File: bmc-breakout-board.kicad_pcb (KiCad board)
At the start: 4 copper layers, 90 x 60 mm, 23 parts, among them J1 PinHeader_2x4, J10 PinHeader_2x4, J11 PinHeader_2x05, J12 61300411121, J13 0473460001, J14 PCIE_BUS_x1, J15 0473460001, J16 PinHeader_1x07, J2 PinHeader_2x13, J3 PinHeader_2x08, J4 61300411121, J5 ME1016813401101, J6 61300411121, J7 DC_SOCKET, J8 PinHeader_2x05, J9 PinHeader_1x07, Q1 BSS138AKA

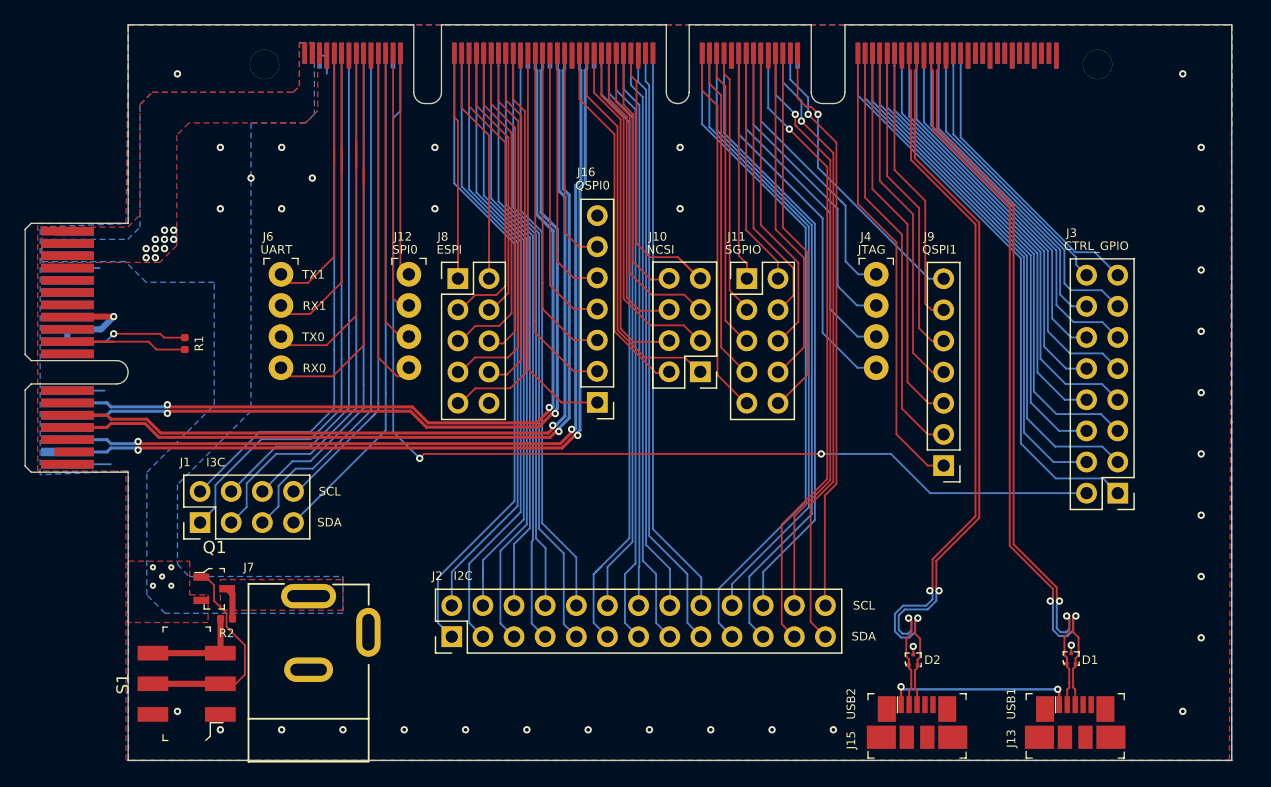
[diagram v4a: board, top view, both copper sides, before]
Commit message: Add mounting holes
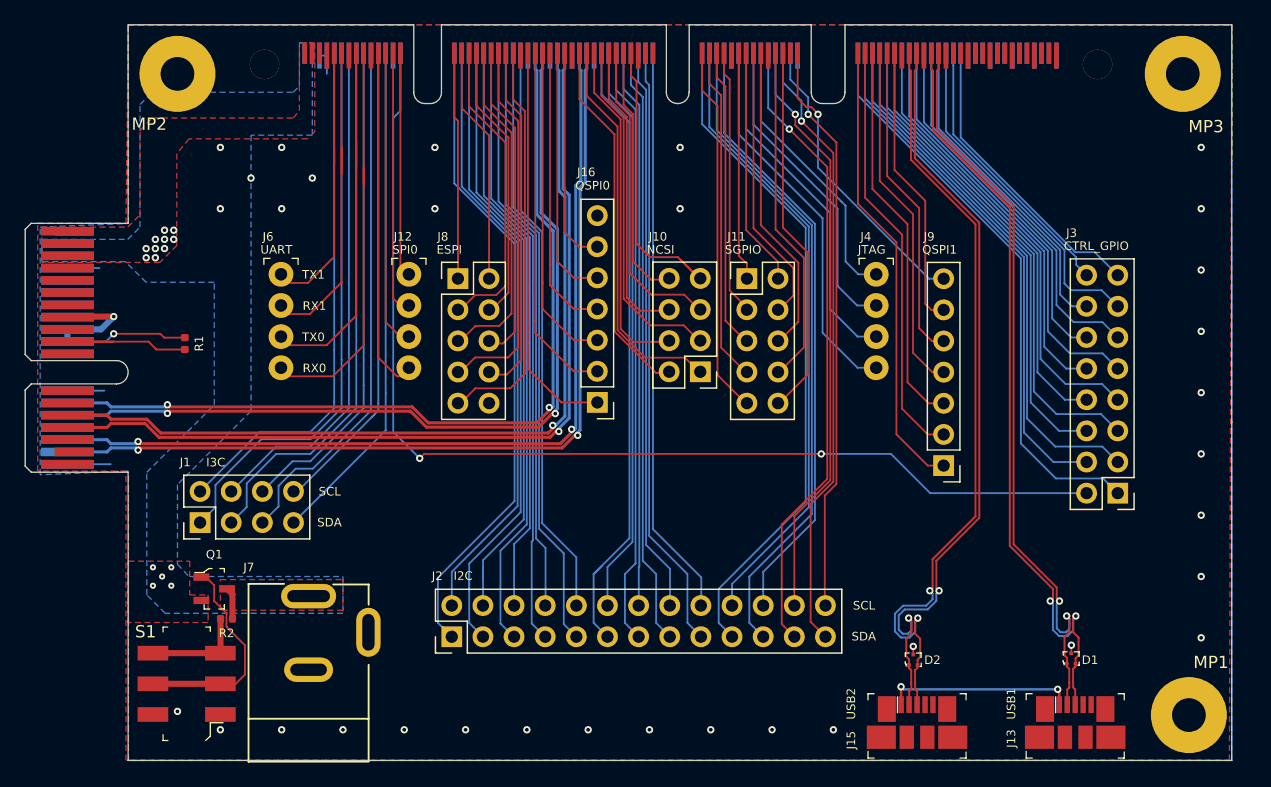
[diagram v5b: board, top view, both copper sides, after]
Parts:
- added MP1: PCB_Mount_Hole_2.5_6.2, bmc-breakout-board-footprints:Mount-hole-M2.5, F.Cu at (146.6, 119.0)
- added MP2: PCB_Mount_Hole_2.5_6.2, bmc-breakout-board-footprints:Mount-hole-M2.5, F.Cu at (64.1, 66.7)
- added MP3: PCB_Mount_Hole_2.5_6.2, bmc-breakout-board-footprints:Mount-hole-M2.5, F.Cu at (146.1, 66.7)
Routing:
- net GND: vias 36 -> 30
- net (no net): vias 0 -> 3
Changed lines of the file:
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@@
     (thickness 1.55)
     (drawings 121)
-    (tracks 905)
+    (tracks 902)
     (zones 0)
-    (modules 23)
+    (modules 26)
     (nets 159)
   )
@@
     (add_net USB2_D_P)
   )
+  (module bmc-breakout-board-footprints:Mount-hole-M2.5 (layer F.Cu)
+    (at 146.1 66.665)
+    (fp_text reference MP3 (at 1.9 4.3) (layer F.SilkS)
+      (effects (font (size 1 1) (thickness 0.15)))
+    )
+    (fp_text value PCB_Mount_Hole_2.5_6.2 (at 0 -0.5) (layer F.Fab)
+      (effects (font (size 1 1) (thickness 0.15)))
+    )
+    (pad 1 thru_hole circle (at 0 0) (size 6.2 6.2) (drill 2.75) (layers *.Cu *.Mask))
+  )
+  (module bmc-breakout-board-footprints:Mount-hole-M2.5 (layer F.Cu)
+    (at 64.1 66.665)
+    (fp_text reference MP2 (at -2.3 4.1) (layer F.SilkS)
+      (effects (font (size 1 1) (thickness 0.15)))
+    )
+    (fp_text value PCB_Mount_Hole_2.5_6.2 (at 0 -0.5) (layer F.Fab)
+      (effects (font (size 1 1) (thickness 0.15)))
+    )
+    (pad 1 thru_hole circle (at 0 0) (size 6.2 6.2) (drill 2.75) (layers *.Cu *.Mask))
+  )
+  (module bmc-breakout-board-footprints:Mount-hole-M2.5 (layer F.Cu)
+    (at 146.6 118.965)
+    (fp_text reference MP1 (at 1.8 -4.3) (layer F.SilkS)
+      (effects (font (size 1 1) (thickness 0.15)))
+    )
+    (fp_text value PCB_Mount_Hole_2.5_6.2 (at 0 -0.5) (layer F.Fab)
+      (effects (font (size 1 1) (thickness 0.15)))
+    )
+    (pad 1 thru_hole circle (at 0 0) (size 6.2 6.2) (drill 2.75) (layers *.Cu *.Mask))
+  )
   (module bmc-breakout-board-footprints:Switch_Slide_JS202011SCQN (layer F.Cu)
     (at 64.85 116.415 90)
     (attr smd)
-    (fp_text reference S1 (at 0 -5.2 90) (layer F.SilkS)
+    (fp_text reference S1 (at 4.25 -3.35 180) (layer F.SilkS)
       (effects (font (size 1 1) (thickness 0.15)))
     )
@@
     (at 67.1 108.665)
     (attr smd)
-    (fp_text reference Q1 (at 0.025 -3.375) (layer F.SilkS)
-      (effects (font (size 1 1) (thickness 0.15)))
+    (fp_text reference Q1 (at 0 -2.8) (layer F.SilkS)
+      (effects (font (size 0.7 0.7) (thickness 0.15)))
     )
     (fp_text value BSS138AKA (at 0.025 3.25) (layer F.Fab)
@@
   (gr_line (start 83.375 62.665) (end 60.075 62.665) (layer Edge.Cuts) (width 0.05))
   (gr_line (start 109.939 122.517) (end 118.929 122.517) (layer B.SilkS) (width 0.12))
-  (via (at 146.1 66.665) (size 0.6) (drill 0.3) (layers F.Cu B.Cu) (net 1))
-  (via (at 146.1 118.665) (size 0.6) (drill 0.3) (layers F.Cu B.Cu) (net 1))
   (via (at 64.1 118.665) (size 0.6) (drill 0.3) (layers F.Cu B.Cu) (net 1))
-  (via (at 64.1 66.665) (size 0.6) (drill 0.3) (layers F.Cu B.Cu) (net 1))
   (via (at 147.6 77.665) (size 0.6) (drill 0.3) (layers F.Cu B.Cu) (net 1))
   (via (at 147.6 82.665) (size 0.6) (drill 0.3) (layers F.Cu B.Cu) (net 1))
@@
   (via (at 67.6 120.165) (size 0.6) (drill 0.3) (layers F.Cu B.Cu) (net 1))
   (via (at 72.6 120.165) (size 0.6) (drill 0.3) (layers F.Cu B.Cu) (net 1))
-  (via (at 67.6 72.665) (size 0.6) (drill 0.3) (layers F.Cu B.Cu) (net 1))
+  (via (at 67.6 72.665) (size 0.6) (drill 0.3) (layers F.Cu B.Cu) (net 0))
   (via (at 72.6 72.665) (size 0.6) (drill 0.3) (layers F.Cu B.Cu) (net 1))
-  (via (at 70.1 75.165) (size 0.6) (drill 0.3) (layers F.Cu B.Cu) (net 1))
+  (via (at 70.1 75.165) (size 0.6) (drill 0.3) (layers F.Cu B.Cu) (net 0))
   (via (at 75.1 75.165) (size 0.6) (drill 0.3) (layers F.Cu B.Cu) (net 1))
-  (via (at 67.6 77.665) (size 0.6) (drill 0.3) (layers F.Cu B.Cu) (net 1))
+  (via (at 67.6 77.665) (size 0.6) (drill 0.3) (layers F.Cu B.Cu) (net 0))
   (via (at 72.6 77.665) (size 0.6) (drill 0.3) (layers F.Cu B.Cu) (net 1))
   (via (at 105.1 77.665) (size 0.6) (drill 0.3) (layers F.Cu B.Cu) (net 1))
@@
     (polygon
       (pts
-        (xy 75.27 69.948648) (xy 74.545 70.665) (xy 70.1 70.665) (xy 70.1 94.165) (xy 64.1 100.165)
-        (xy 64.1 106.665) (xy 65.045 107.665) (xy 77.6 107.665) (xy 77.6 110.665) (xy 63.1 110.665)
-        (xy 61.6 109.165) (xy 61.6 99.165) (xy 67.1 93.665) (xy 67.1 83.665) (xy 61.545 83.665)
-        (xy 59.85 81.975) (xy 53.045 81.975) (xy 53.045 80.165) (xy 60.045 80.165) (xy 61.045 79.165)
-        (xy 61.045 69.165) (xy 62.045 68.165) (xy 73.545 68.165) (xy 74.045 67.665) (xy 74.05 64.115)
-        (xy 75.27 64.115)
+        (xy 75.1 71.665) (xy 70.1 71.665) (xy 70.1 94.165) (xy 64.1 100.165) (xy 64.1 106.665)
+        (xy 65.045 107.665) (xy 77.6 107.665) (xy 77.6 110.665) (xy 63.1 110.665) (xy 61.6 109.165)
+        (xy 61.6 99.165) (xy 67.1 93.665) (xy 67.1 83.665) (xy 61.545 83.665) (xy 59.85 81.975)
+        (xy 53.045 81.975) (xy 53.045 80.165) (xy 60.045 80.165) (xy 61.045 79.165) (xy 61.045 69.165)
+        (xy 62.045 68.165) (xy 73.545 68.165) (xy 74.045 67.665) (xy 74.05 64.115) (xy 75.1 64.115)
       )
     )
@@
     (polygon
       (pts
-        (xy 75.545 69.665) (xy 74.545 70.665) (xy 65.045 70.665) (xy 64.045 71.665) (xy 64.045 80.665)
+        (xy 75.3 71.365) (xy 74.7 71.965) (xy 65.045 71.965) (xy 64.045 73.165) (xy 64.045 80.665)
         (xy 62.66 82.045) (xy 53.045 82.045) (xy 53.045 79.165) (xy 60.045 79.165) (xy 61.045 78.165)
-        (xy 61.045 69.165) (xy 62.045 68.165) (xy 73.545 68.165) (xy 74.045 67.665) (xy 74.045 64.165)
-        (xy 75.545 64.165)
+        (xy 61.045 71.265) (xy 62.045 70.265) (xy 73.545 70.265) (xy 74.045 69.665) (xy 74.045 64.165)
+        (xy 75.3 64.165)
       )
     )

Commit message: Add descriptions on the silkscreen layer
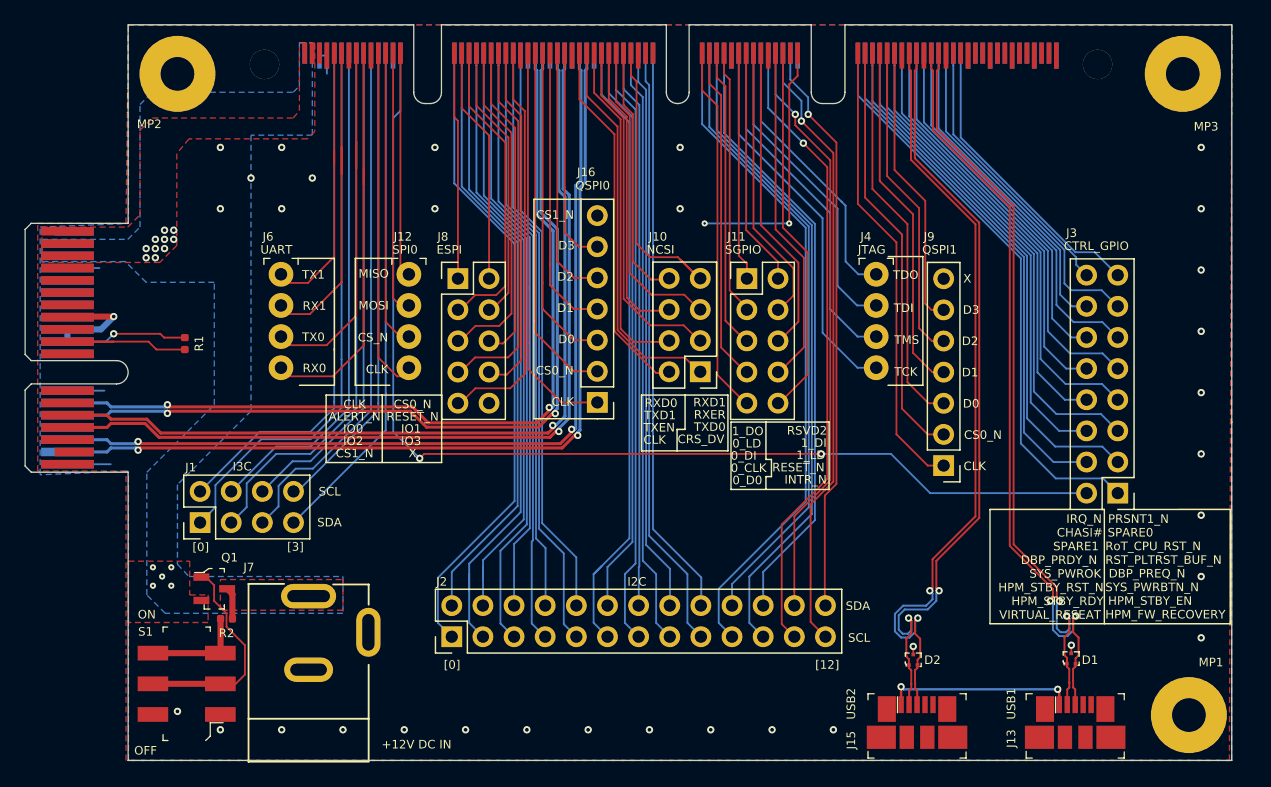
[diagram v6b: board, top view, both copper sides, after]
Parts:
- MP1, MP2, MP3: footprint bmc-breakout-board-footprints:Mount-hole-M2.5 -> antmicro-footprints:Mount-hole-M2.5
- Q1: footprint bmc-breakout-board-footprints:SOT-23-3 -> antmicro-footprints:SOT-23-3
- R2: footprint bmc-breakout-board-footprints:0402-res -> antmicro-footprints:0402-res
- S1: footprint bmc-breakout-board-footprints:Switch_Slide_JS202011SCQN -> antmicro-footprints:Switch_Slide_JS202011SCQN
- moved N1 1.88 mm to (94.5, 102.5)
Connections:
- J16 pad 7: Net-(J16-Pad7) -> QSPI0_CS1_N
- J9 pad 7: QSPI0_CS1_N -> Net-(J9-Pad7)
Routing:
- net QSPI0_CS1_N: track 24.3 -> 30.1 mm, vias 1 -> 2
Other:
- board text added: "+12V DC IN"
- board text added: "0_CLK"
- board text added: "0_D0"
- board text added: "0_DI"
- board text added: "0_LD"
- board text added: "1_DI"
- board text added: "1_DO"
- board text added: "1_LD"
- board text added: "ALERT_N"
- board text added: "CHASI#"
- board text added: "CLK"
- board text added: "CRS_DV"
- board text added: "CS0_N"
- board text added: "CS1_N"
- board text added: "CS_N"
- board text added: "D0"
- board text added: "D1"
- board text added: "D2"
- board text added: "D3"
- board text added: "DBP_PRDY_N"
- board text added: "DBP_PREQ_N"
- board text added: "HPM_FW_RECOVERY"
- board text added: "HPM_STBY_EN"
- board text added: "HPM_STBY_RDY"
- board text added: "HPM_STBY_RST_N"
- board text added: "INTR_N"
- board text added: "IO0"
- board text added: "IO1"
- board text added: "IO2"
- board text added: "IO3"
- board text added: "IRQ_N"
- board text added: "MISO"
- board text added: "MOSI"
- board text added: "OFF"
- board text added: "ON"
- board text added: "PRSNT1_N"
- board text added: "RESET_N"
- board text added: "RST_PLTRST_BUF_N"
- board text added: "RSVD2"
- board text added: "RXD0"
- board text added: "RXD1"
- board text added: "RXER"
- board text added: "RoT_CPU_RST_N"
- board text added: "SPARE0"
- board text added: "SPARE1"
- board text added: "SYS_PWRBTN_N"
- board text added: "SYS_PWROK"
- board text added: "TCK"
- board text added: "TDI"
- board text added: "TDO"
- board text added: "TMS"
- board text added: "TXD0"
- board text added: "TXD1"
- board text added: "TXEN"
- board text added: "VIRTUAL_RESEAT"
- board text added: "X"
- board text added: "[0]"
- board text added: "[12]"
- board text added: "[3]"

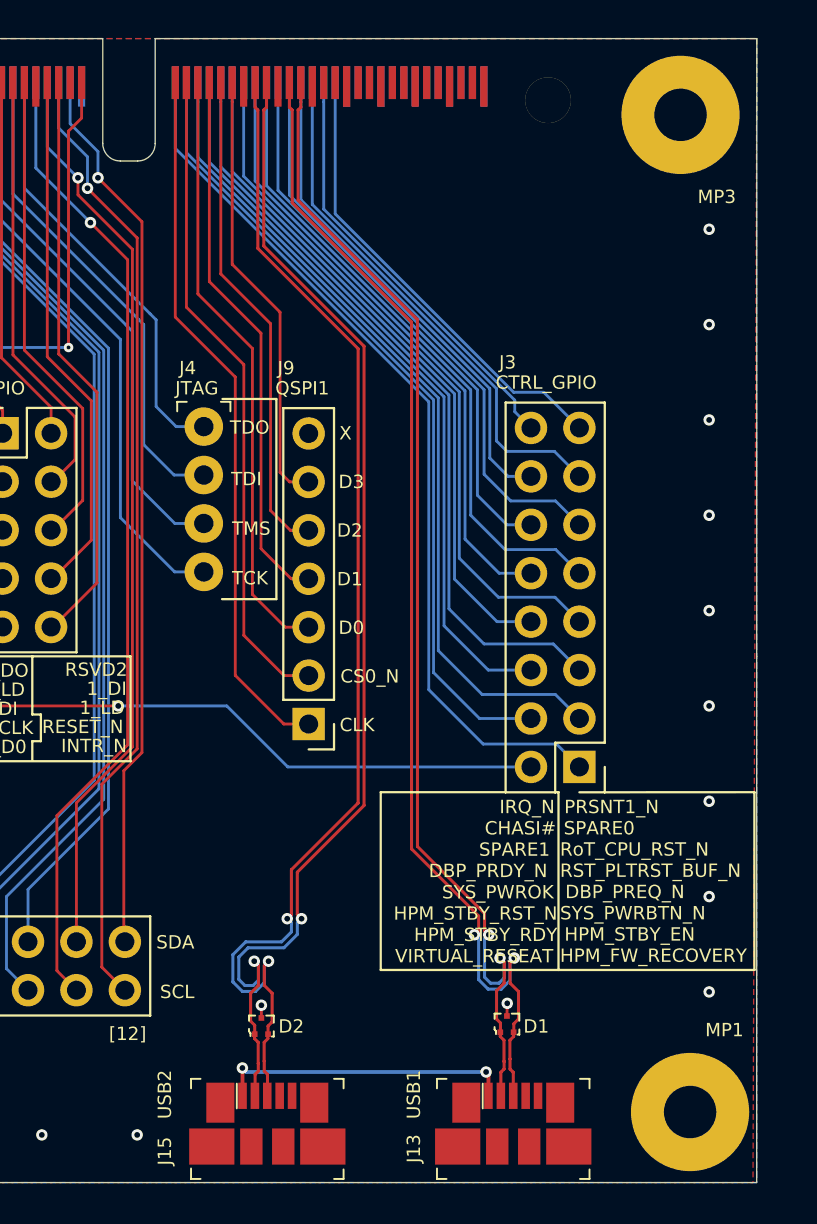
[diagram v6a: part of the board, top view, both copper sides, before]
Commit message: Replace host USB with USB A
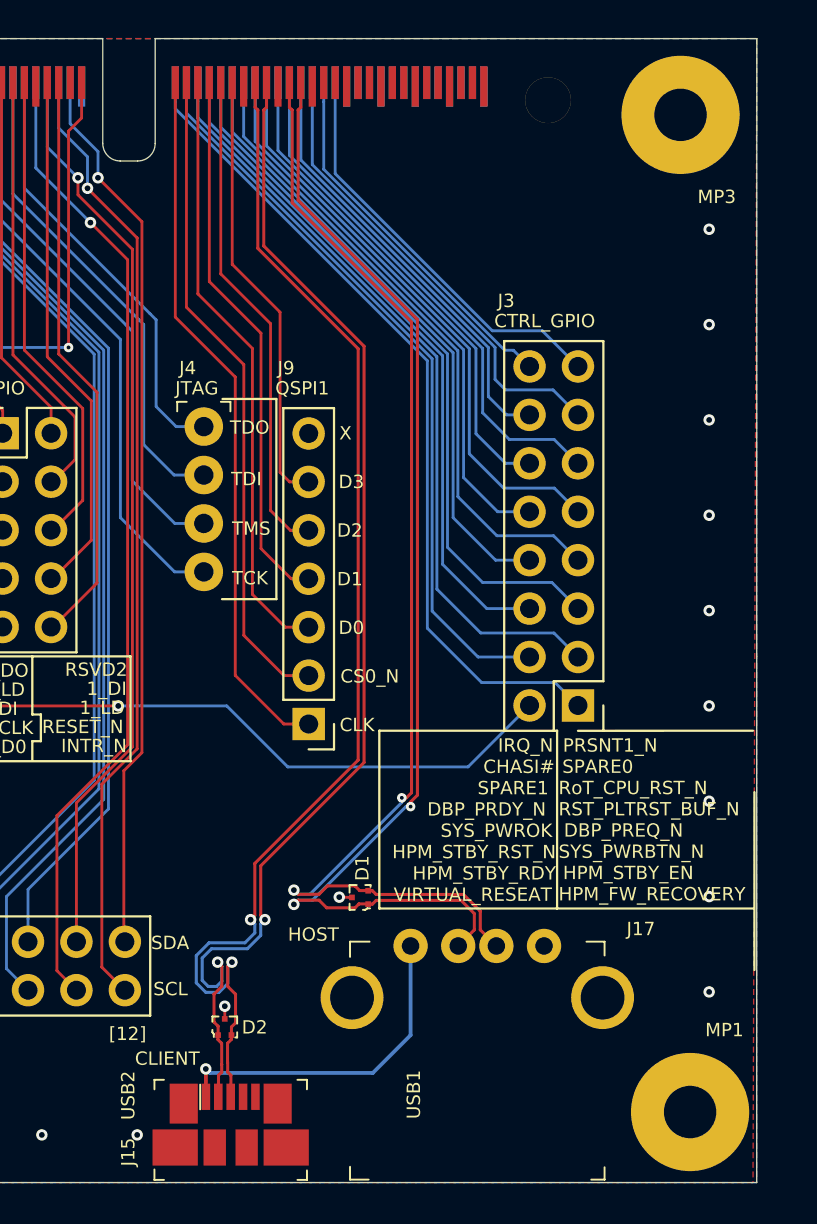
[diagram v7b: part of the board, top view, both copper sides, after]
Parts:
- removed J13: 0473460001, bmc-breakout-board-footprints:USB_Micro_B_Female_0473460001
- added J17: UE27AC54100, bmc-breakout-board-footprints:USB_A_Female_UE27AC54100, F.Cu at (135.4, 113.0)
- MP1, MP2, MP3: footprint antmicro-footprints:Mount-hole-M2.5 -> bmc-breakout-board-footprints:Mount-hole-M2.5
- Q1: footprint antmicro-footprints:SOT-23-3 -> bmc-breakout-board-footprints:SOT-23-3
- R2: footprint antmicro-footprints:0402-res -> bmc-breakout-board-footprints:0402-res
- S1: footprint antmicro-footprints:Switch_Slide_JS202011SCQN -> bmc-breakout-board-footprints:Switch_Slide_JS202011SCQN
- moved D1 10.2 mm to (129.3, 107.7), turned to 90 degrees
- moved J3 3.23 mm to (140.7, 97.6)
- moved D2 1.92 mm to (122.2, 114.5)
- moved J15 1.92 mm to (122.5, 120.8)
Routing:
- net HPM_STBY_RDY: track 42.4 -> 39.2 mm
- net HPM_STBY_EN: track 43.9 -> 40.6 mm
- net DBP_PREQ_N: track 37.3 -> 34.0 mm
- net SYS_PWRBTN_N: track 40.7 -> 37.5 mm
- net RoT_CPU_RST_N: track 30.9 -> 27.6 mm
- net SYS_PWROK: track 35.8 -> 32.5 mm
- net SPARE0: track 27.9 -> 24.7 mm
- net HPM_STBY_RST_N: track 39.1 -> 35.9 mm
- net SPARE1: track 29.4 -> 26.2 mm
- net RST_PLTRST_BUF_N: track 34.1 -> 30.8 mm
- net HPM_FW_RECOVERY: track 46.9 -> 43.7 mm
- net DBP_PRDY_N: track 32.7 -> 29.4 mm
- net CHASI#: track 26.4 -> 23.1 mm
- net IRQ_N: track 22.6 -> 19.6 mm
- net PRSNT1_N: track 24.3 -> 21.7 mm
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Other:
- board text added: "CLIENT"
- board text added: "HOST"
